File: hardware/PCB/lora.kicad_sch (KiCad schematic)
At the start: 23 parts, among them U10 SX1261IMLTRT, U11 BGS12P2L6E6327XT, Y2 32.00 MHz

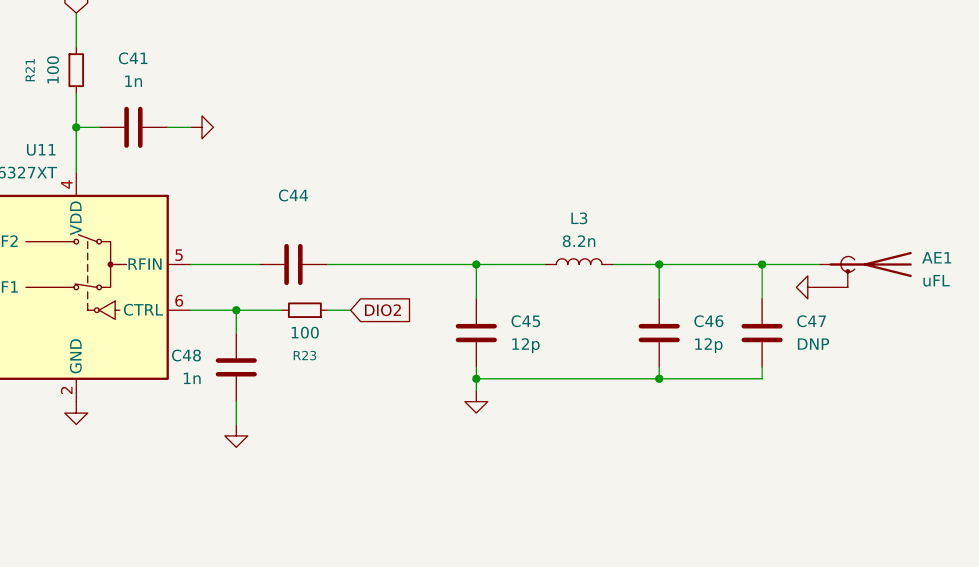
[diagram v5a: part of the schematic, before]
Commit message: Finished parts sourcing and added missing footprints
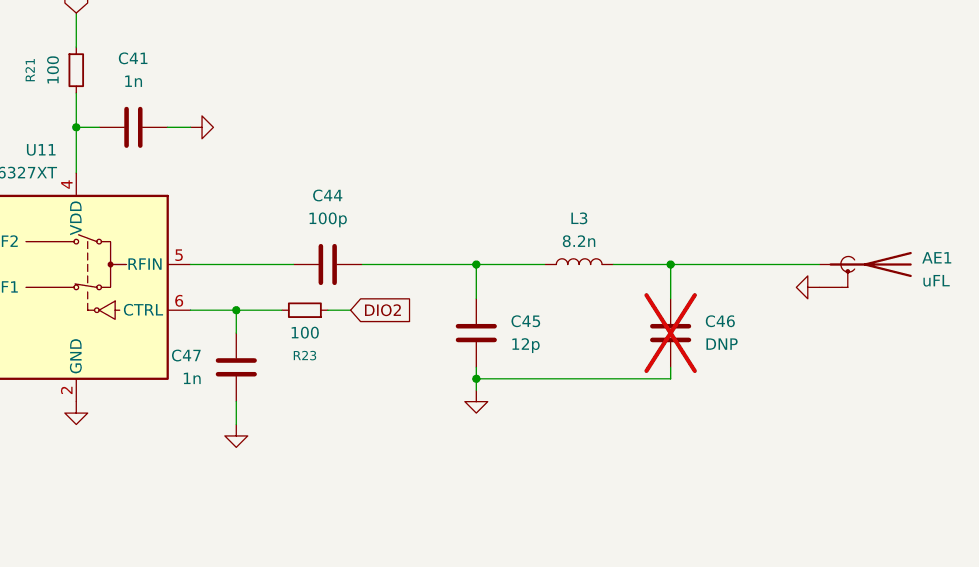
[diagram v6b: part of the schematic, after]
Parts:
- removed C46: 12p, symbol Device:C
- AE1: footprint (none) -> Connector_Coaxial:U.FL_Hirose_U.FL-R-SMT-1_Vertical
- C38, C39, C40, C41, C42, C45: footprint (none) -> Capacitor_SMD:C_1206_3216Metric_Pad1.33x1.80mm_HandSolder
- C43: footprint (none) -> Capacitor_SMD:C_1210_3225Metric_Pad1.33x2.70mm_HandSolder
- C44: value ~ -> 100p; footprint (none) -> Capacitor_SMD:C_1206_3216Metric_Pad1.33x1.80mm_HandSolder
- C46: renamed from C47; footprint (none) -> Capacitor_SMD:C_1206_3216Metric_Pad1.33x1.80mm_HandSolder; now not fitted
- C47: renamed from C48; footprint (none) -> Capacitor_SMD:C_1206_3216Metric_Pad1.33x1.80mm_HandSolder
- L1: footprint (none) -> Inductor_SMD:L_1812_4532Metric_Pad1.30x3.40mm_HandSolder
- L2, L3: footprint (none) -> Inductor_SMD:L_1008_2520Metric_Pad1.43x2.20mm_HandSolder
- R21, R22, R23, R24: footprint (none) -> Resistor_SMD:R_1206_3216Metric_Pad1.30x1.75mm_HandSolder
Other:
- moved on the sheet: C44
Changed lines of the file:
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@@
 	)
 	(junction
-		(at 237.49 85.09)
-		(diameter 0)
-		(color 0 0 0 0)
-	)
-	(junction
 		(at 72.39 49.53)
 		(diameter 0)
@@
 	)
 	(junction
-		(at 226.06 97.79)
+		(at 205.74 85.09)
 		(diameter 0)
 		(color 0 0 0 0)
 	)
 	(junction
-		(at 205.74 85.09)
+		(at 227.33 85.09)
 		(diameter 0)
 		(color 0 0 0 0)
@@
 	)
 	(junction
-		(at 226.06 85.09)
-		(diameter 0)
-		(color 0 0 0 0)
-	)
-	(junction
 		(at 161.29 69.85)
 		(diameter 0)
@@
 	(wire
 		(pts
-			(xy 226.06 85.09) (xy 237.49 85.09)
+			(xy 220.98 85.09) (xy 227.33 85.09)
 		)
 		(stroke
@@
 	(wire
 		(pts
-			(xy 220.98 85.09) (xy 226.06 85.09)
-		)
-		(stroke
-			(width 0)
-			(type default)
-		)
-	)
-	(wire
-		(pts
 			(xy 50.8 99.06) (xy 62.23 99.06)
 		)
@@
 	(wire
 		(pts
-			(xy 237.49 96.52) (xy 237.49 97.79)
+			(xy 227.33 96.52) (xy 227.33 97.79)
 		)
 		(stroke
@@
 	(wire
 		(pts
-			(xy 226.06 96.52) (xy 226.06 97.79)
-		)
-		(stroke
-			(width 0)
-			(type default)
-		)
-	)
-	(wire
-		(pts
-			(xy 189.23 85.09) (xy 205.74 85.09)
+			(xy 193.04 85.09) (xy 205.74 85.09)
 		)
 		(stroke
@@
 	(wire
 		(pts
-			(xy 226.06 97.79) (xy 237.49 97.79)
-		)
-		(stroke
-			(width 0)
-			(type default)
-		)
-	)
-	(wire
-		(pts
 			(xy 82.55 53.34) (xy 82.55 55.88)
 		)
@@
 	(wire
 		(pts
-			(xy 173.99 85.09) (xy 181.61 85.09)
+			(xy 173.99 85.09) (xy 185.42 85.09)
 		)
 		(stroke
@@
 	(wire
 		(pts
-			(xy 226.06 85.09) (xy 226.06 88.9)
-		)
-		(stroke
-			(width 0)
-			(type default)
-		)
-	)
-	(wire
-		(pts
 			(xy 142.24 82.55) (xy 148.59 82.55)
 		)
@@
 	(wire
 		(pts
-			(xy 205.74 97.79) (xy 226.06 97.79)
+			(xy 205.74 97.79) (xy 227.33 97.79)
 		)
 		(stroke
@@
 	(wire
 		(pts
-			(xy 237.49 85.09) (xy 243.84 85.09)
+			(xy 30.48 60.96) (xy 30.48 71.12)
 		)
 		(stroke
@@
 	(wire
 		(pts
-			(xy 30.48 60.96) (xy 30.48 71.12)
+			(xy 227.33 85.09) (xy 227.33 88.9)
 		)
 		(stroke
@@
 	(wire
 		(pts
-			(xy 237.49 85.09) (xy 237.49 88.9)
+			(xy 179.07 90.17) (xy 179.07 92.71)
 		)
 		(stroke
@@
 	(wire
 		(pts
-			(xy 179.07 90.17) (xy 179.07 92.71)
+			(xy 43.18 68.58) (xy 62.23 68.58)
 		)
 		(stroke
@@
 	(wire
 		(pts
-			(xy 43.18 68.58) (xy 62.23 68.58)
+			(xy 227.33 85.09) (xy 243.84 85.09)
 		)
 		(stroke
@@
 			)
 		)
-		(property "Footprint" ""
+		(property "Footprint" "Capacitor_SMD:C_1206_3216Metric_Pad1.33x1.80mm_HandSolder"
 			(at 171.45 68.8848 0)
 			(effects
@@
 			)
 		)
-		(property "Footprint" ""
+		(property "Footprint" "Inductor_SMD:L_1812_4532Metric_Pad1.30x3.40mm_HandSolder"
 			(at 100.33 71.12 0)
 			(effects
@@
 			)
 		)
-		(property "Footprint" ""
+		(property "Footprint" "Resistor_SMD:R_1206_3216Metric_Pad1.30x1.75mm_HandSolder"
 			(at 186.69 90.17 0)
 			(effects
@@
 			)
 		)
-		(property "Footprint" ""
+		(property "Footprint" "Capacitor_SMD:C_1206_3216Metric_Pad1.33x1.80mm_HandSolder"
 			(at 96.52 78.74 0)
 			(effects
@@
 			)
 		)
-		(property "Footprint" ""
+		(property "Footprint" "Resistor_SMD:R_1206_3216Metric_Pad1.30x1.75mm_HandSolder"
 			(at 161.29 63.5 0)
 			(effects
@@
 		(on_board yes)
 		(dnp no)
-		(property "Reference" "C48"
+		(property "Reference" "C47"
 			(at 175.26 95.2499 0)
 			(effects
@@
 			)
 		)
-		(property "Footprint" ""
+		(property "Footprint" "Capacitor_SMD:C_1206_3216Metric_Pad1.33x1.80mm_HandSolder"
 			(at 180.0352 92.71 0)
 			(effects
@@
 			(project "Startracker"
 				(path "/45ea479c-a8ef-4c14-88b0-391ede4fd156/efc52d26-5e7f-40f5-a09a-58b8b5321559"
-					(reference "C48")
+					(reference "C47")
 					(unit 1)
 				)
@@
 			)
 		)
-		(property "Footprint" ""
+		(property "Footprint" "Capacitor_SMD:C_1206_3216Metric_Pad1.33x1.80mm_HandSolder"
 			(at 204.7748 88.9 0)
 			(effects
@@
 			)
 		)
-		(property "Footprint" ""
+		(property "Footprint" "Capacitor_SMD:C_1206_3216Metric_Pad1.33x1.80mm_HandSolder"
 			(at 62.23 50.4952 0)
 			(effects
@@
 	(symbol
 		(lib_id "Device:C")
-		(at 185.42 85.09 90)
+		(at 189.23 85.09 90)
 		(unit 1)
 		(exclude_from_sim no)
@@
 		(fields_autoplaced yes)
 		(property "Reference" "C44"
-			(at 185.42 77.47 90)
+			(at 189.23 77.47 90)
 			(effects
 				(font
@@
 			)
 		)
-		(property "Value" "~"
-			(at 185.42 80.01 90)
+		(property "Value" "100p"
+			(at 189.23 80.01 90)
 			(effects
 				(font
@@
 			)
 		)
-		(property "Footprint" ""
-			(at 189.23 84.1248 0)
+		(property "Footprint" "Capacitor_SMD:C_1206_3216Metric_Pad1.33x1.80mm_HandSolder"
+			(at 193.04 84.1248 0)
 			(effects
 				(font
@@
 		)
 		(property "Datasheet" "~"
-			(at 185.42 85.09 0)
+			(at 189.23 85.09 0)
 			(effects
 				(font
@@
 		)
 		(property "Description" "Unpolarized capacitor"
-			(at 185.42 85.09 0)
+			(at 189.23 85.09 0)
 			(effects
 				(font
@@
 			)
 		)
-		(property "Footprint" ""
+		(property "Footprint" "Resistor_SMD:R_1206_3216Metric_Pad1.30x1.75mm_HandSolder"
 			(at 45.72 75.438 90)
 			(effects
@@
 			)
 		)
-		(property "Footprint" ""
+		(property "Footprint" "Resistor_SMD:R_1206_3216Metric_Pad1.30x1.75mm_HandSolder"
 			(at 55.372 110.49 90)
 			(effects
@@
 			)
 		)
-		(property "Footprint" ""
+		(property "Footprint" "Capacitor_SMD:C_1210_3225Metric_Pad1.33x2.70mm_HandSolder"
 			(at 104.14 78.74 0)
 			(effects
@@
 			)
 		)
-		(property "Footprint" ""
+		(property "Footprint" "Inductor_SMD:L_1008_2520Metric_Pad1.43x2.20mm_HandSolder"
 			(at 217.17 85.09 0)
 			(effects
@@
 			)
 		)
-		(property "Footprint" ""
+		(property "Footprint" "Inductor_SMD:L_1008_2520Metric_Pad1.43x2.20mm_HandSolder"
 			(at 111.76 80.01 0)
 			(effects
@@
 			)
 		)
-		(property "Footprint" ""
+		(property "Footprint" "Connector_Coaxial:U.FL_Hirose_U.FL-R-SMT-1_Vertical"
 			(at 251.46 85.09 0)
 			(effects
@@
 	(symbol
 		(lib_id "Device:C")
-		(at 237.49 92.71 180)
+		(at 227.33 92.71 180)
 		(unit 1)
 		(exclude_from_sim yes)
 		(in_bom no)
 		(on_board yes)
-		(dnp no)
+		(dnp yes)
 		(fields_autoplaced yes)
-		(property "Reference" "C47"
-			(at 241.3 91.4399 0)
+		(property "Reference" "C46"
+			(at 231.14 91.4399 0)
 			(effects
 				(font
@@
 		)
 		(property "Value" "DNP"
-			(at 241.3 93.9799 0)
+			(at 231.14 93.9799 0)
 			(effects
 				(font
@@
 			)
 		)
-		(property "Footprint" ""
-			(at 236.5248 88.9 0)
+		(property "Footprint" "Capacitor_SMD:C_1206_3216Metric_Pad1.33x1.80mm_HandSolder"
+			(at 226.3648 88.9 0)
 			(effects
 				(font
@@
 		)
 		(property "Datasheet" "~"
-			(at 237.49 92.71 0)
+			(at 227.33 92.71 0)
 			(effects
 				(font
@@
 		)
 		(property "Description" "Unpolarized capacitor"
-			(at 237.49 92.71 0)
+			(at 227.33 92.71 0)
 			(effects
 				(font
@@
 			(project "Startracker"
 				(path "/45ea479c-a8ef-4c14-88b0-391ede4fd156/efc52d26-5e7f-40f5-a09a-58b8b5321559"
-					(reference "C47")
+					(reference "C46")
 					(unit 1)
 				)
@@
 			)
 		)
-		(property "Footprint" ""
+		(property "Footprint" "Capacitor_SMD:C_1206_3216Metric_Pad1.33x1.80mm_HandSolder"
 			(at 92.71 48.5648 0)
 			(effects
@@
 	(symbol
 		(lib_id "Device:C")
-		(at 226.06 92.71 180)
-		(unit 1)
-		(exclude_from_sim no)
-		(in_bom yes)
-		(on_board yes)
-		(dnp no)
-		(fields_autoplaced yes)
-		(property "Reference" "C46"
-			(at 229.87 91.4399 0)
-			(effects
-				(font
-					(size 1.27 1.27)
-				)
-				(justify right)
-			)
-		)
-		(property "Value" "12p"
-			(at 229.87 93.9799 0)
-			(effects
-				(font
-					(size 1.27 1.27)
-				)
-				(justify right)
-			)
-		)
-		(property "Footprint" ""
-			(at 225.0948 88.9 0)
-			(effects
-				(font
-					(size 1.27 1.27)
-				)
-				(hide yes)
-			)
-		)
-		(property "Datasheet" "~"
-			(at 226.06 92.71 0)
-			(effects
-				(font
-					(size 1.27 1.27)
-				)
-				(hide yes)
-			)
-		)
-		(property "Description" "Unpolarized capacitor"
-			(at 226.06 92.71 0)
-			(effects
-				(font
-					(size 1.27 1.27)
-				)
-				(hide yes)
-			)
-		)
-		(pin "2"
-		)
-		(pin "1"
-		)
-		(instances
-			(project "Startracker"
-				(path "/45ea479c-a8ef-4c14-88b0-391ede4fd156/efc52d26-5e7f-40f5-a09a-58b8b5321559"
-					(reference "C46")
-					(unit 1)
-				)
-			)
-		)
-	)
-	(symbol
-		(lib_id "Device:C")
 		(at 113.03 69.85 90)
 		(unit 1)
@@
 			)
 		)
-		(property "Footprint" ""
+		(property "Footprint" "Capacitor_SMD:C_1206_3216Metric_Pad1.33x1.80mm_HandSolder"
 			(at 116.84 68.8848 0)
 			(effects
